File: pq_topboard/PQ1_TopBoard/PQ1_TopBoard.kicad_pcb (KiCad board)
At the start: 2 copper layers, 50 x 50 mm, 20 parts, among them IC1 TCN75AVUA713, J1 Conn_01x11_MountingPin

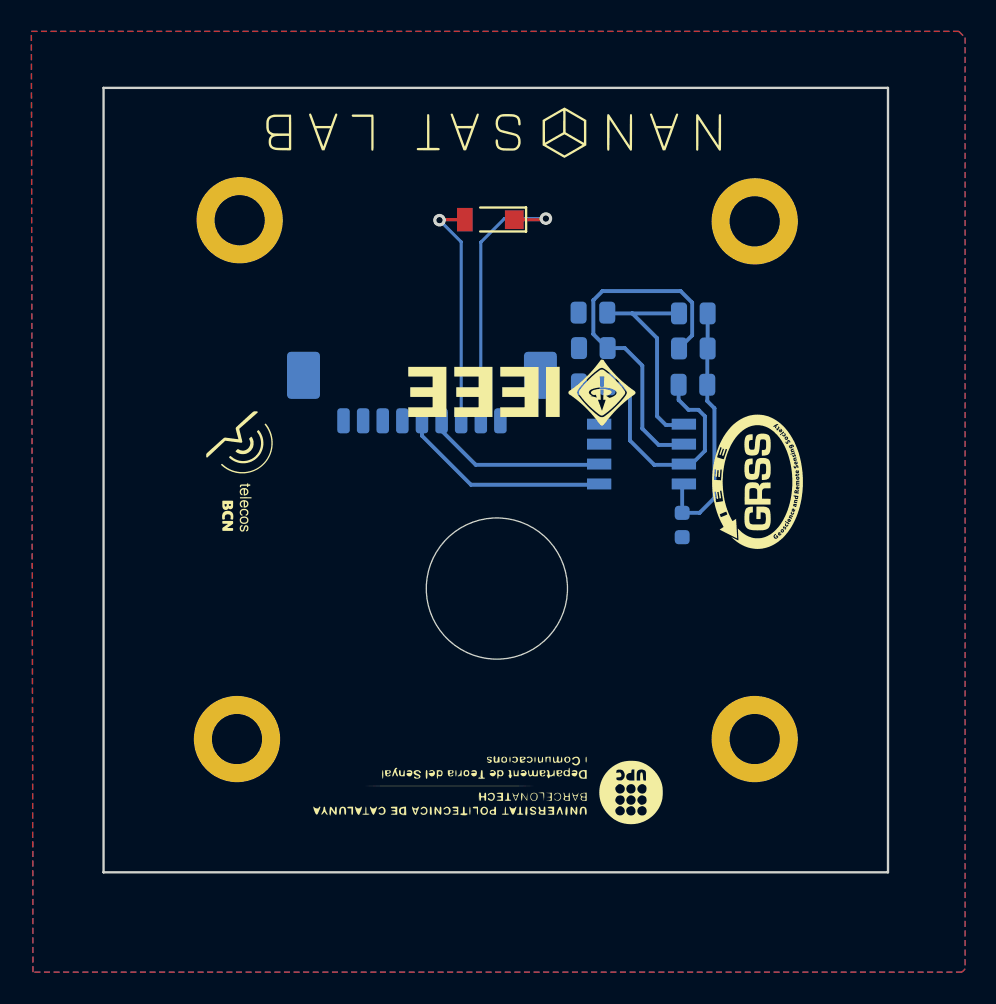
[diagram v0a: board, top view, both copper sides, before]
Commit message: solved collission in PL1
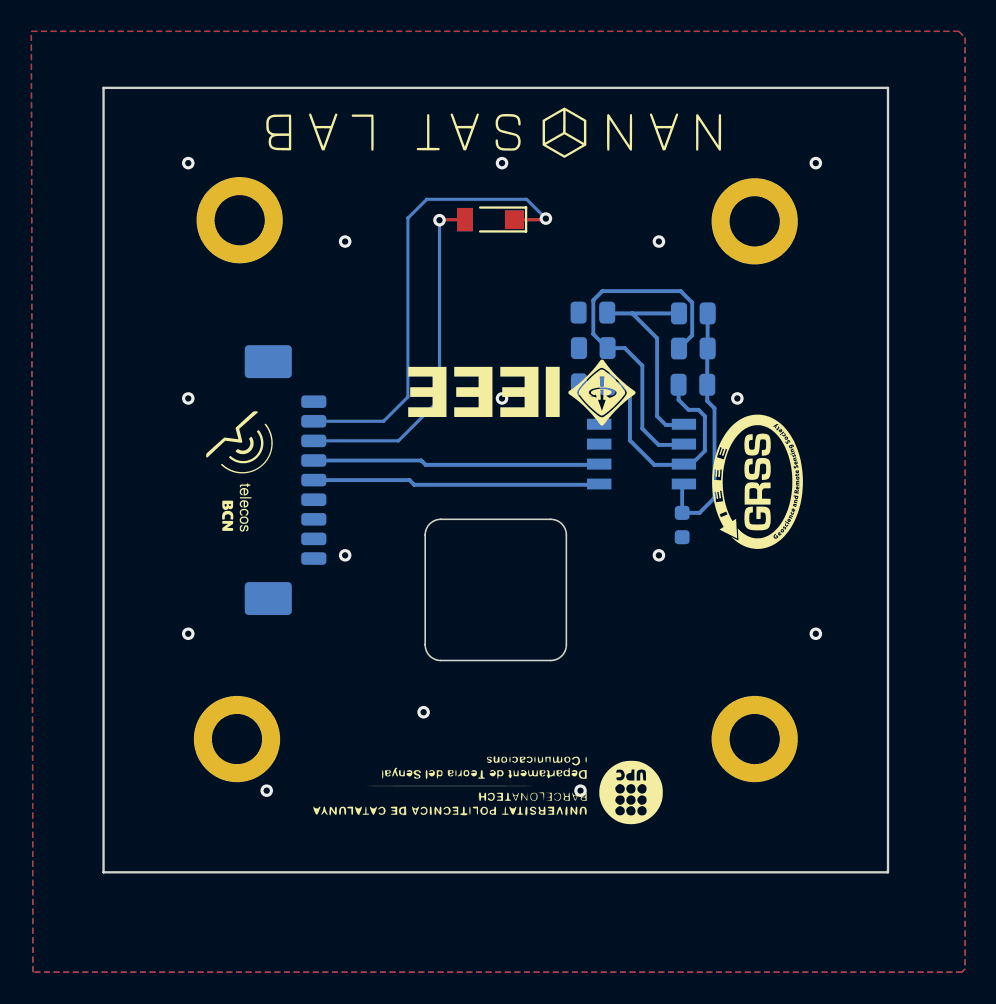
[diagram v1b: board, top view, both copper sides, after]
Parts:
- removed H5: MountingHole, MountingHole:MountingHole_8.4mm_M8
- moved J1 11.2 mm to (88.8, 58.3), turned to 90 degrees
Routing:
- net /PH+: track 18.2 -> 29.9 mm
- net /PH-: track 15.0 -> 22.2 mm
- net /SCL: track 11.6 -> 18.4 mm
- net /SDA: track 13.6 -> 18.4 mm
- net GND: vias 0 -> 15
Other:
- outline, holes or cut-outs redrawn

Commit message: solved collission in PL1
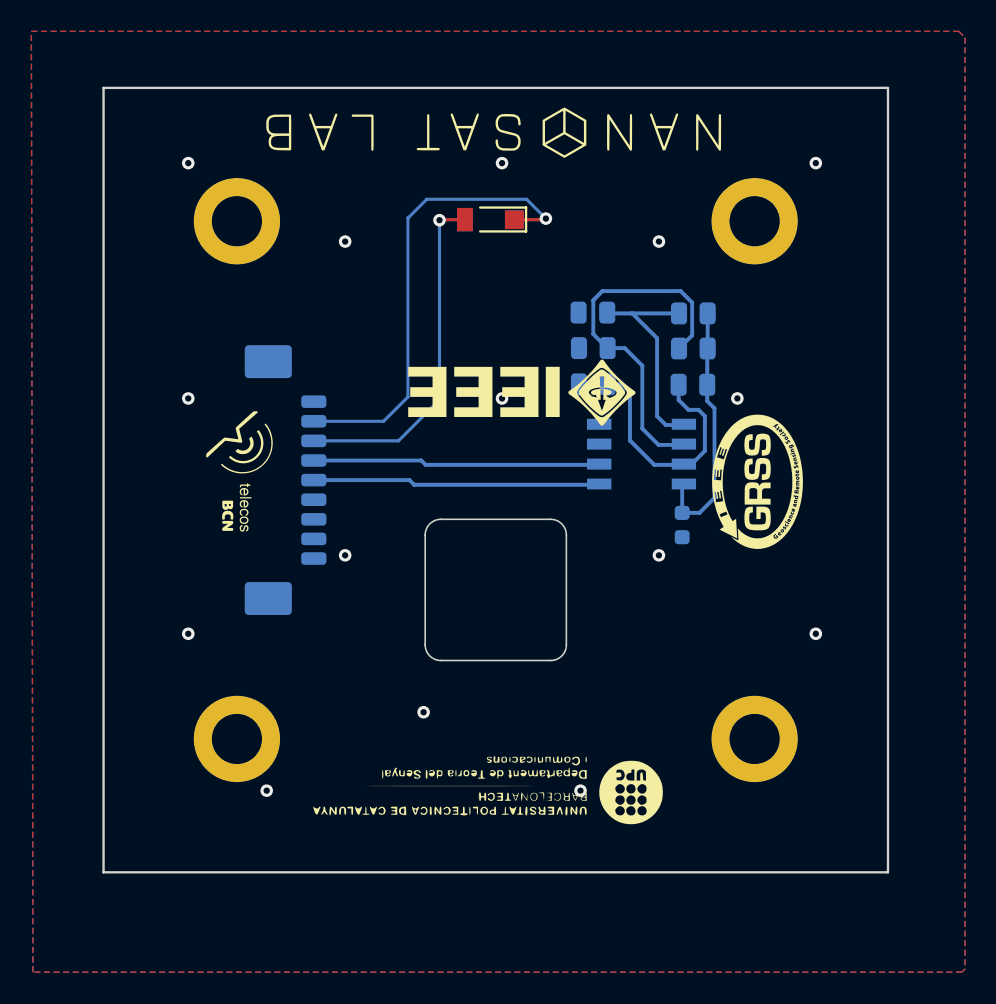
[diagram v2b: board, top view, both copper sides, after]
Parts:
- moved H1 0.19 mm to (86.3, 41.8)
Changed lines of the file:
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@@
   )
   (footprint "MountingHole:MountingHole_3.2mm_M3_ISO14580_Pad" (layer "F.Cu")
-    (at 86.4325 41.7089)
+    (at 86.256 41.774)
     (descr "Mounting Hole 3.2mm, M3, ISO14580")
     (tags "mounting hole 3.2mm m3 iso14580")
@@
   )
   (footprint "MountingHole:MountingHole_3.2mm_M3_ISO14580_Pad" (layer "F.Cu")
-    (at 119.26 41.78)
+    (at 119.256 41.774)
     (descr "Mounting Hole 3.2mm, M3, ISO14580")
     (tags "mounting hole 3.2mm m3 iso14580")
@@
     (attr exclude_from_pos_files)
     (fp_text reference "H2" (at 0 -3.75 unlocked) (layer "B.SilkS") hide
-        (effects (font (size 0.4 0.4) (thickness 0.15)) (justify mirror))
+        (effects (font (size 0.4 0.4) (thickness 0.1)) (justify mirror))
     )
     (fp_text value "MountingHole_Pad" (at 0 3.75) (layer "F.Fab")
@@
   )
   (footprint "MountingHole:MountingHole_3.2mm_M3_ISO14580_Pad" (layer "F.Cu")
-    (at 119.26 74.78)
+    (at 119.256 74.774)
     (descr "Mounting Hole 3.2mm, M3, ISO14580")
     (tags "mounting hole 3.2mm m3 iso14580")
@@
     (attr exclude_from_pos_files)
     (fp_text reference "H3" (at 0 -3.75 unlocked) (layer "B.SilkS") hide
-        (effects (font (size 0.4 0.4) (thickness 0.15)) (justify mirror))
+        (effects (font (size 0.4 0.4) (thickness 0.1)) (justify mirror))
     )
     (fp_text value "MountingHole_Pad" (at 0 3.75) (layer "F.Fab")
@@
   )
   (footprint "MountingHole:MountingHole_3.2mm_M3_ISO14580_Pad" (layer "F.Cu")
-    (at 86.26 74.78)
+    (at 86.256 74.774)
     (descr "Mounting Hole 3.2mm, M3, ISO14580")
     (tags "mounting hole 3.2mm m3 iso14580")
@@
     (attr exclude_from_pos_files)
     (fp_text reference "H4" (at 0 -3.75 unlocked) (layer "B.SilkS") hide
-        (effects (font (size 0.4 0.4) (thickness 0.15)) (justify mirror))
+        (effects (font (size 0.4 0.4) (thickness 0.1)) (justify mirror))
     )
     (fp_text value "MountingHole_Pad" (at 0 3.75) (layer "F.Fab")
@@
   (gr_line (start 77.756 33.274) (end 127.756 33.274)
     (stroke (width 0.15) (type solid)) (layer "Edge.Cuts"))
-  (gr_rect (start 79.756 81.274) (end 125.756 35.274)
+  (gr_rect (start 79.756 35.274) (end 125.756 81.274)
     (stroke (width 0.05) (type default)) (fill none) (layer "B.CrtYd"))
-  (gr_rect (start 92.756 71.774) (end 112.956 43.774)
+  (gr_rect (start 92.756 43.774) (end 112.956 71.774)
     (stroke (width 0.05) (type default)) (fill none) (layer "B.CrtYd"))
   (gr_text "TOP BOARD PQ1" (at 115.0178 75.2602) (layer "B.SilkS")
@@
   )
   (dimension (type aligned) (layer "Cmts.User")
+    (pts (xy 119.256 41.774) (xy 119.256 74.774))
+    (height -12.1)
+    (gr_text "33.0000 mm" (at 130.206 58.274 90) (layer "Cmts.User")
+      (effects (font (size 1 1) (thickness 0.15)))
+    )
+    (format (prefix "") (suffix "") (units 3) (units_format 1) (precision 4))
+    (style (thickness 0.15) (arrow_length 1.27) (text_position_mode 0) (extension_height 0.58642) (extension_offset 0.5) keep_text_aligned)
+  )
+  (dimension (type aligned) (layer "Cmts.User")
+    (pts (xy 86.256 41.774) (xy 119.256 41.774))
+    (height -11.7)
+    (gr_text "33.0000 mm" (at 102.756 28.924) (layer "Cmts.User")
+      (effects (font (size 1 1) (thickness 0.15)))
+    )
+    (format (prefix "") (suffix "") (units 3) (units_format 1) (precision 4))
+    (style (thickness 0.15) (arrow_length 1.27) (text_position_mode 0) (extension_height 0.58642) (extension_offset 0.5) keep_text_aligned)
+  )
+  (dimension (type aligned) (layer "Cmts.User")
+    (pts (xy 119.256 74.774) (xy 86.256 74.774))
+    (height -13.6)
+    (gr_text "33.0000 mm" (at 102.756 87.224) (layer "Cmts.User")
+      (effects (font (size 1 1) (thickness 0.15)))
+    )
+    (format (prefix "") (suffix "") (units 3) (units_format 1) (precision 4))
+    (style (thickness 0.15) (arrow_length 1.27) (text_position_mode 0) (extension_height 0.58642) (extension_offset 0.5) keep_text_aligned)
+  )
+  (dimension (type aligned) (layer "Cmts.User")
+    (pts (xy 86.256 74.774) (xy 86.256 41.774))
+    (height -13.9)
+    (gr_text "33.0000 mm" (at 71.206 58.274 90) (layer "Cmts.User")
+      (effects (font (size 1 1) (thickness 0.15)))
+    )
+    (format (prefix "") (suffix "") (units 3) (units_format 1) (precision 4))
+    (style (thickness 0.15) (arrow_length 1.27) (text_position_mode 0) (extension_height 0.58642) (extension_offset 0.5) keep_text_aligned)
+  )
+  (dimension (type aligned) (layer "Cmts.User")
     (pts (xy 127.756 83.274) (xy 127.756 33.274))
-    (height 8)
-    (gr_text "50.0000 mm" (at 133.956 58.274 90) (layer "Cmts.User")
+    (height 12.1)
+    (gr_text "50.0000 mm" (at 138.056 58.274 90) (layer "Cmts.User")
       (effects (font (size 1.5 1.5) (thickness 0.3)))
     )

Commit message: solved collission in PL1
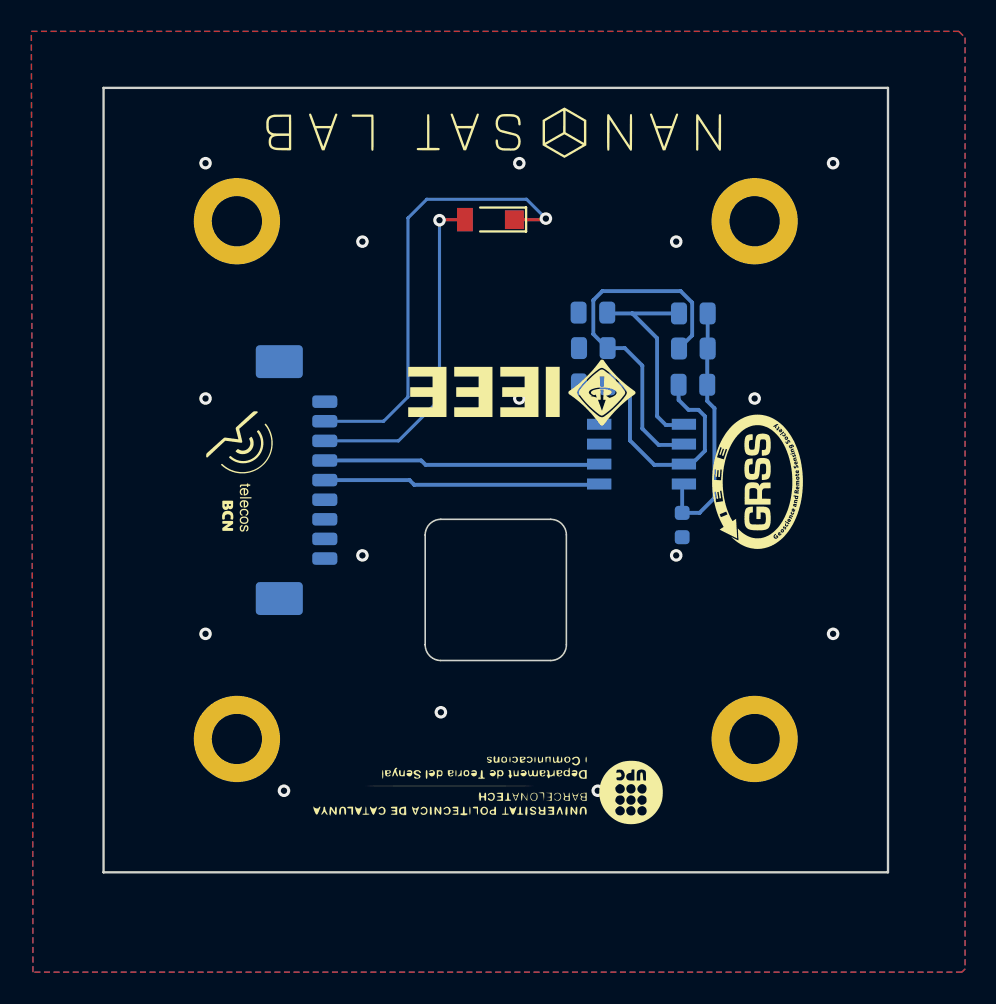
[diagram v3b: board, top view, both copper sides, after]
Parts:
- moved J1 0.70 mm to (89.5, 58.3)
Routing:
- net /SDA: track 18.4 -> 17.7 mm
- net /SCL: track 18.4 -> 17.7 mm
- net /PH-: track 22.2 -> 21.5 mm
- net /PH+: track 29.9 -> 29.2 mm
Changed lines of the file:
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@@
   )
   (footprint "Connector_Molex:Molex_PicoBlade_53261-0971_1x09-1MP_P1.25mm_Horizontal" (layer "B.Cu")
-    (at 88.756 58.274 90)
+    (at 89.456 58.274 90)
     (descr "Molex PicoBlade series connector, 53261-0971 (http://www.molex.com/pdm_docs/sd/532610271_sd.pdf), generated with kicad-footprint-generator")
     (tags "connector Molex PicoBlade top entry")
@@
     (style (thickness 0.2) (arrow_length 1.27) (text_position_mode 0) (extension_height 0.58642) (extension_offset 0.5) keep_text_aligned)
   )
-  (via (at 98.155 73.07) (size 0.8) (drill 0.4) (layers "F.Cu" "B.Cu") (free) (net 1))
-  (via (at 93.155 63.07) (size 0.8) (drill 0.4) (layers "F.Cu" "B.Cu") (free) (net 1))
-  (via (at 103.155 38.07) (size 0.8) (drill 0.4) (layers "F.Cu" "B.Cu") (free) (net 1))
-  (via (at 88.155 78.07) (size 0.8) (drill 0.4) (layers "F.Cu" "B.Cu") (free) (net 1))
-  (via (at 113.155 43.07) (size 0.8) (drill 0.4) (layers "F.Cu" "B.Cu") (free) (net 1))
-  (via (at 113.155 63.07) (size 0.8) (drill 0.4) (layers "F.Cu" "B.Cu") (free) (net 1))
-  (via (at 83.155 68.07) (size 0.8) (drill 0.4) (layers "F.Cu" "B.Cu") (free) (net 1))
-  (via (at 118.155 53.07) (size 0.8) (drill 0.4) (layers "F.Cu" "B.Cu") (free) (net 1))
-  (via (at 83.155 53.07) (size 0.8) (drill 0.4) (layers "F.Cu" "B.Cu") (free) (net 1))
-  (via (at 123.155 68.07) (size 0.8) (drill 0.4) (layers "F.Cu" "B.Cu") (free) (net 1))
-  (via (at 83.155 38.07) (size 0.8) (drill 0.4) (layers "F.Cu" "B.Cu") (free) (net 1))
-  (via (at 93.155 43.07) (size 0.8) (drill 0.4) (layers "F.Cu" "B.Cu") (free) (net 1))
-  (via (at 103.155 53.07) (size 0.8) (drill 0.4) (layers "F.Cu" "B.Cu") (free) (net 1))
-  (via (at 123.155 38.07) (size 0.8) (drill 0.4) (layers "F.Cu" "B.Cu") (free) (net 1))
-  (via (at 108.155 78.07) (size 0.8) (drill 0.4) (layers "F.Cu" "B.Cu") (free) (net 1))
+  (via (at 99.256 73.074) (size 0.8) (drill 0.4) (layers "F.Cu" "B.Cu") (free) (net 1))
+  (via (at 94.256 63.074) (size 0.8) (drill 0.4) (layers "F.Cu" "B.Cu") (free) (net 1))
+  (via (at 104.256 38.074) (size 0.8) (drill 0.4) (layers "F.Cu" "B.Cu") (free) (net 1))
+  (via (at 89.256 78.074) (size 0.8) (drill 0.4) (layers "F.Cu" "B.Cu") (free) (net 1))
+  (via (at 114.256 43.074) (size 0.8) (drill 0.4) (layers "F.Cu" "B.Cu") (free) (net 1))
+  (via (at 114.256 63.074) (size 0.8) (drill 0.4) (layers "F.Cu" "B.Cu") (free) (net 1))
+  (via (at 84.256 68.074) (size 0.8) (drill 0.4) (layers "F.Cu" "B.Cu") (free) (net 1))
+  (via (at 119.256 53.074) (size 0.8) (drill 0.4) (layers "F.Cu" "B.Cu") (free) (net 1))
+  (via (at 84.256 53.074) (size 0.8) (drill 0.4) (layers "F.Cu" "B.Cu") (free) (net 1))
+  (via (at 124.256 68.074) (size 0.8) (drill 0.4) (layers "F.Cu" "B.Cu") (free) (net 1))
+  (via (at 84.256 38.074) (size 0.8) (drill 0.4) (layers "F.Cu" "B.Cu") (free) (net 1))
+  (via (at 94.256 43.074) (size 0.8) (drill 0.4) (layers "F.Cu" "B.Cu") (free) (net 1))
+  (via (at 104.256 53.074) (size 0.8) (drill 0.4) (layers "F.Cu" "B.Cu") (free) (net 1))
+  (via (at 124.256 38.074) (size 0.8) (drill 0.4) (layers "F.Cu" "B.Cu") (free) (net 1))
+  (via (at 109.256 78.074) (size 0.8) (drill 0.4) (layers "F.Cu" "B.Cu") (free) (net 1))
   (segment (start 99.1985 41.6765) (end 99.1682 41.7068) (width 0.2) (layer "F.Cu") (net 2))
   (segment (start 100.7885 41.6765) (end 99.1985 41.6765) (width 0.2) (layer "F.Cu") (net 2))
   (via (at 99.1682 41.7068) (size 0.8) (drill 0.4) (layers "F.Cu" "B.Cu") (free) (net 2))
-  (segment (start 91.156 55.774) (end 96.556 55.774) (width 0.2) (layer "B.Cu") (net 2))
   (segment (start 96.556 55.774) (end 99.1682 53.1618) (width 0.2) (layer "B.Cu") (net 2))
   (segment (start 99.1682 53.1618) (end 99.1682 41.7068) (width 0.2) (layer "B.Cu") (net 2))
+  (segment (start 96.556 55.774) (end 91.856 55.774) (width 0.2) (layer "B.Cu") (net 2))
   (segment (start 103.9385 41.6765) (end 105.8787 41.6765) (width 0.2) (layer "F.Cu") (net 3))
   (segment (start 105.8787 41.6765) (end 105.95 41.6052) (width 0.2) (layer "F.Cu") (net 3))
@@
   (segment (start 97.156 52.974) (end 97.156 41.574) (width 0.2) (layer "B.Cu") (net 3))
   (segment (start 97.156 41.574) (end 98.356 40.374) (width 0.2) (layer "B.Cu") (net 3))
-  (segment (start 91.156 54.524) (end 95.606 54.524) (width 0.2) (layer "B.Cu") (net 3))
+  (segment (start 91.856 54.524) (end 95.606 54.524) (width 0.2) (layer "B.Cu") (net 3))
   (segment (start 104.7188 40.374) (end 105.95 41.6052) (width 0.2) (layer "B.Cu") (net 3))
   (segment (start 97.256 58.274) (end 97.5544 58.5724) (width 0.25) (layer "B.Cu") (net 4))
+  (segment (start 97.256 58.274) (end 91.856 58.274) (width 0.25) (layer "B.Cu") (net 4))
   (segment (start 97.5544 58.5724) (end 109.3956 58.5724) (width 0.25) (layer "B.Cu") (net 4))
-  (segment (start 91.156 58.274) (end 97.256 58.274) (width 0.25) (layer "B.Cu") (net 4))
-  (segment (start 91.156 57.024) (end 98.006 57.024) (width 0.25) (layer "B.Cu") (net 5))
   (segment (start 98.2844 57.3024) (end 109.3956 57.3024) (width 0.25) (layer "B.Cu") (net 5))
   (segment (start 98.006 57.024) (end 98.2844 57.3024) (width 0.25) (layer "B.Cu") (net 5))
+  (segment (start 98.006 57.024) (end 91.856 57.024) (width 0.25) (layer "B.Cu") (net 5))
   (segment (start 116.6942 53.6956) (end 116.2351 53.2365) (width 0.25) (layer "B.Cu") (net 6))
   (segment (start 114.6368 60.3628) (end 115.742 60.3628) (width 0.25) (layer "B.Cu") (net 6))

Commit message: Added NSL lektron logo, reconciled library symbol - footprints, moved the picoblade connector so not to conflict with the top structure, fixed VCC trace issue
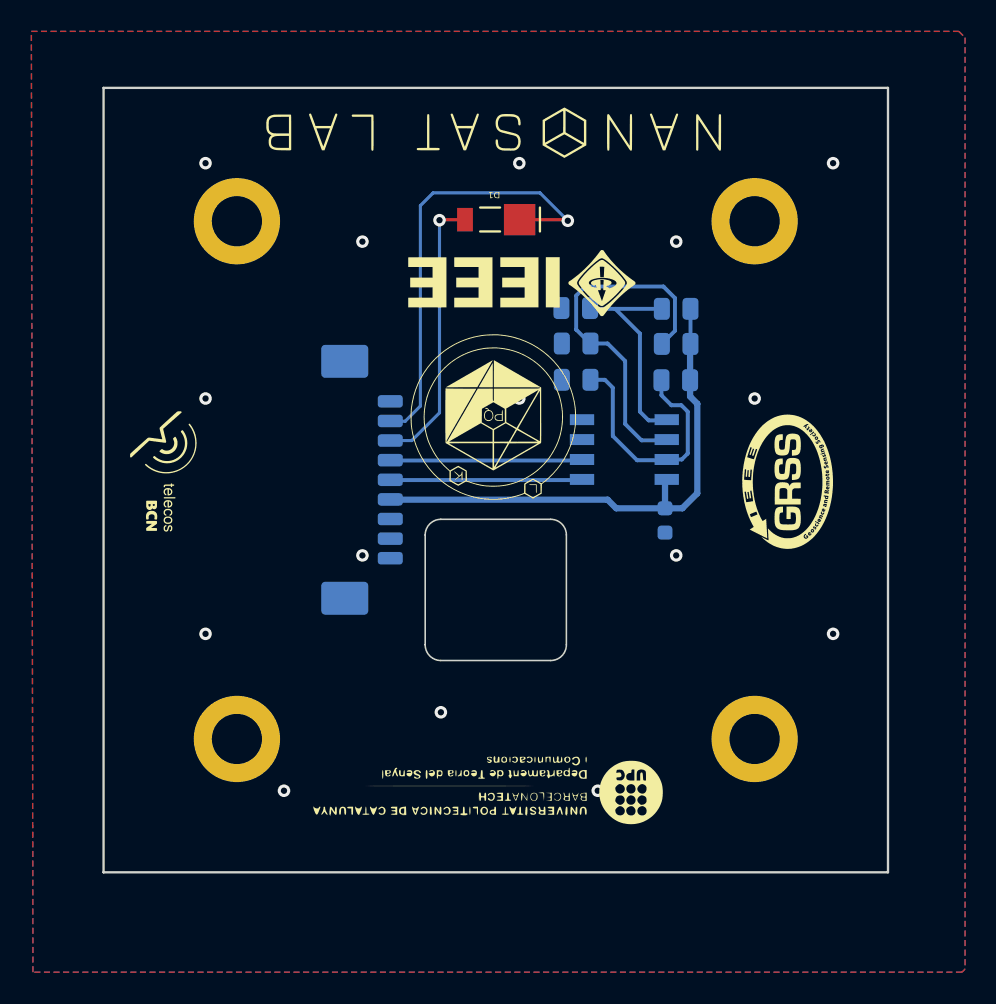
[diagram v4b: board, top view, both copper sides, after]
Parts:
- added Annotation6: Silkscreen_Annotation, symbols-nsl:NSL_Lektron, F.Cu at (102.6, 54.2)
- Annotation1: footprint -nsl_symbols:IEEE_logo -> symbols-nsl:IEEE_logo
- Annotation2: footprint -nsl_symbols:GRSS -> symbols-nsl:GRSS
- Annotation3: footprint -nsl_symbols:NSL_long -> symbols-nsl:NSL_long
- Annotation4: footprint -nsl_symbols:Telecos -> symbols-nsl:Telecos
- Annotation5: footprint -nsl_symbols:UPC_positiu -> symbols-nsl:UPC_positiu
- D1: footprint -nsl_passive:SLCD-61N8 -> passive-nsl:SLCD-61N8
- IC1: footprint -nsl_sensor:TCN75AVOA -> sensor-nsl:TCN75AVOA
- moved Annotation1 6.98 mm to (102.9, 45.7)
- moved Annotation4 4.85 mm to (81.5, 58.0)
- moved J1 4.18 mm to (93.6, 58.3)
- moved Annotation2 1.92 mm to (121.4, 58.4)
- moved C1 1.13 mm to (113.5, 60.8)
- moved GA1 1.13 mm to (107.9, 49.6), turned to 180 degrees
- moved GA2 1.13 mm to (107.9, 47.3), turned to 180 degrees
- moved IC1 1.13 mm to (110.9, 56.4)
- moved VA0 1.13 mm to (114.2, 51.9)
- moved GA0 1.13 mm to (107.9, 51.9), turned to 180 degrees
- moved VA1 1.13 mm to (114.3, 49.6)
- moved VA2 1.13 mm to (114.3, 47.4)
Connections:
- C1 pad 1: /VCC -> /3V3_PERM
- GA0 pad 1: GND -> Net-(IC1-A0)
- GA0 pad 2: Net-(IC1-A0) -> GND
- GA1 pad 1: GND -> Net-(IC1-A1)
- GA1 pad 2: Net-(IC1-A1) -> GND
- GA2 pad 1: GND -> Net-(IC1-A2)
- GA2 pad 2: Net-(IC1-A2) -> GND
- IC1 pad 8: /VCC -> /3V3_PERM
- VA0 pad 2: /VCC -> /3V3_PERM
- VA1 pad 2: /VCC -> /3V3_PERM
- VA2 pad 2: /VCC -> /3V3_PERM
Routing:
- net /3V3_PERM: track 0.00 -> 33.9 mm
- net /VCC: track 16.2 -> 0.00 mm
- net /SDA: track 17.7 -> 12.2 mm
- net /SCL: track 17.7 -> 12.3 mm
- net /PH-: track 21.5 -> 17.8 mm
- net Net-(IC1-A0): track 14.9 -> 15.9 mm
